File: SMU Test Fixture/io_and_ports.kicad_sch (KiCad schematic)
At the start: 50 parts, among them J1 AD2 Connector, J10 Ext. Source, J12 105-1102-001, J2 Scope -1, J3 Scope +1, J4 Scope -2, J5 Scope +2, J6 WG1, J7 WG2, J8 AD2 Connector, J9 105-1102-001, U10 ADGS1412, U11 ADGS1412, U8 ADGS1412, U9 ADGS1412

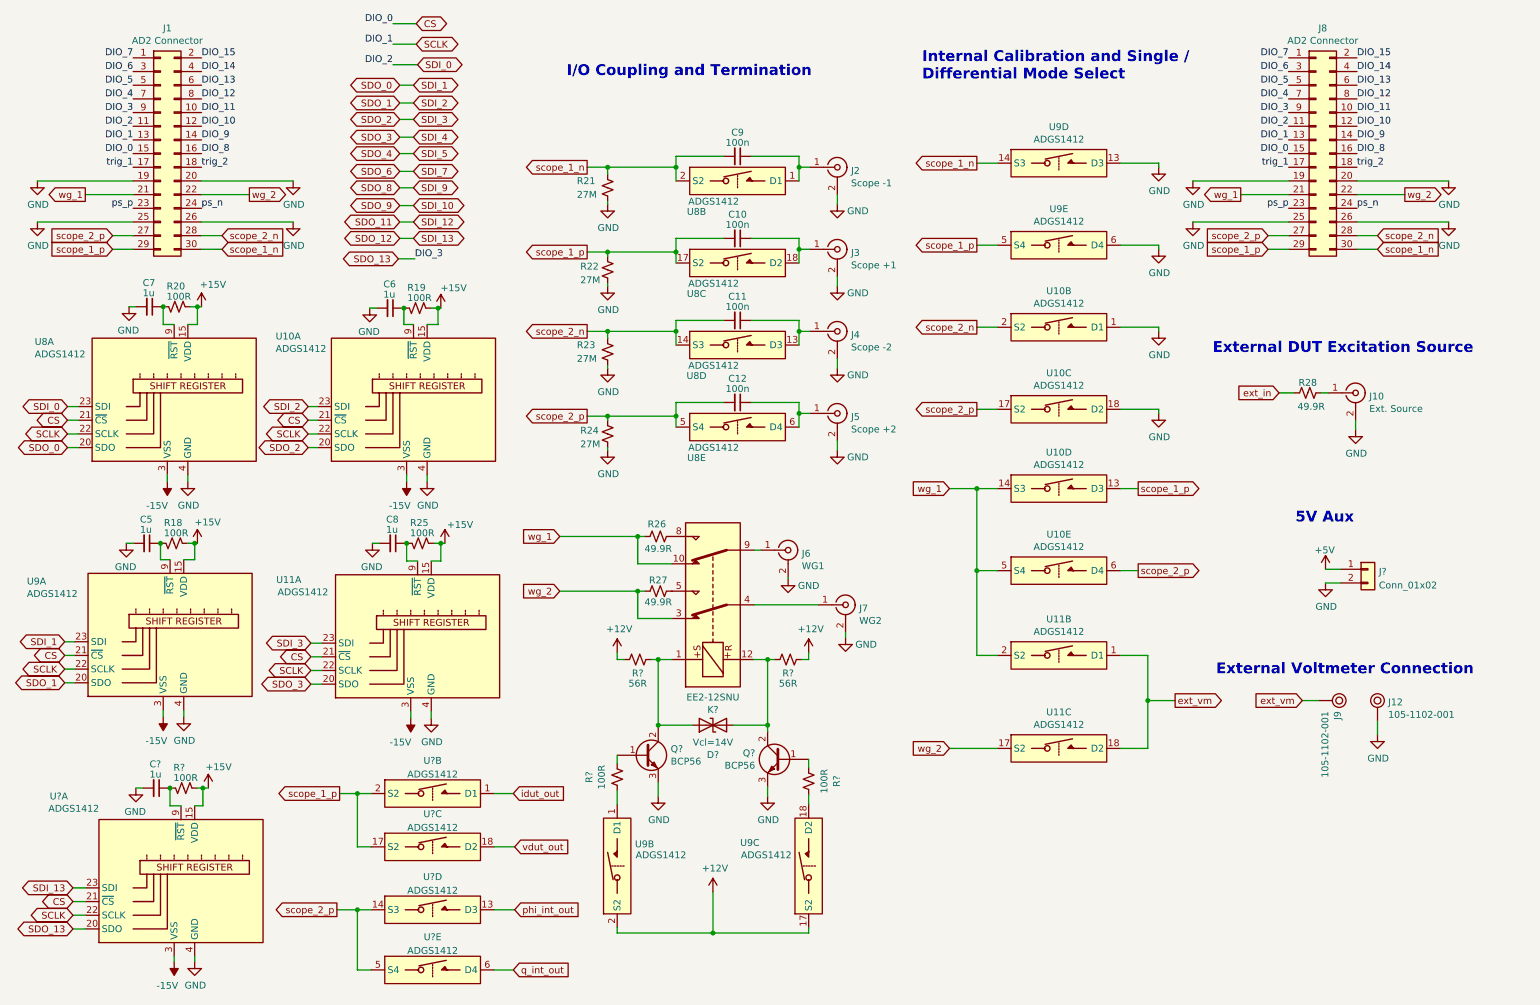
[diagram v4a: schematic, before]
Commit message: Finish adding bypass for all a.switches
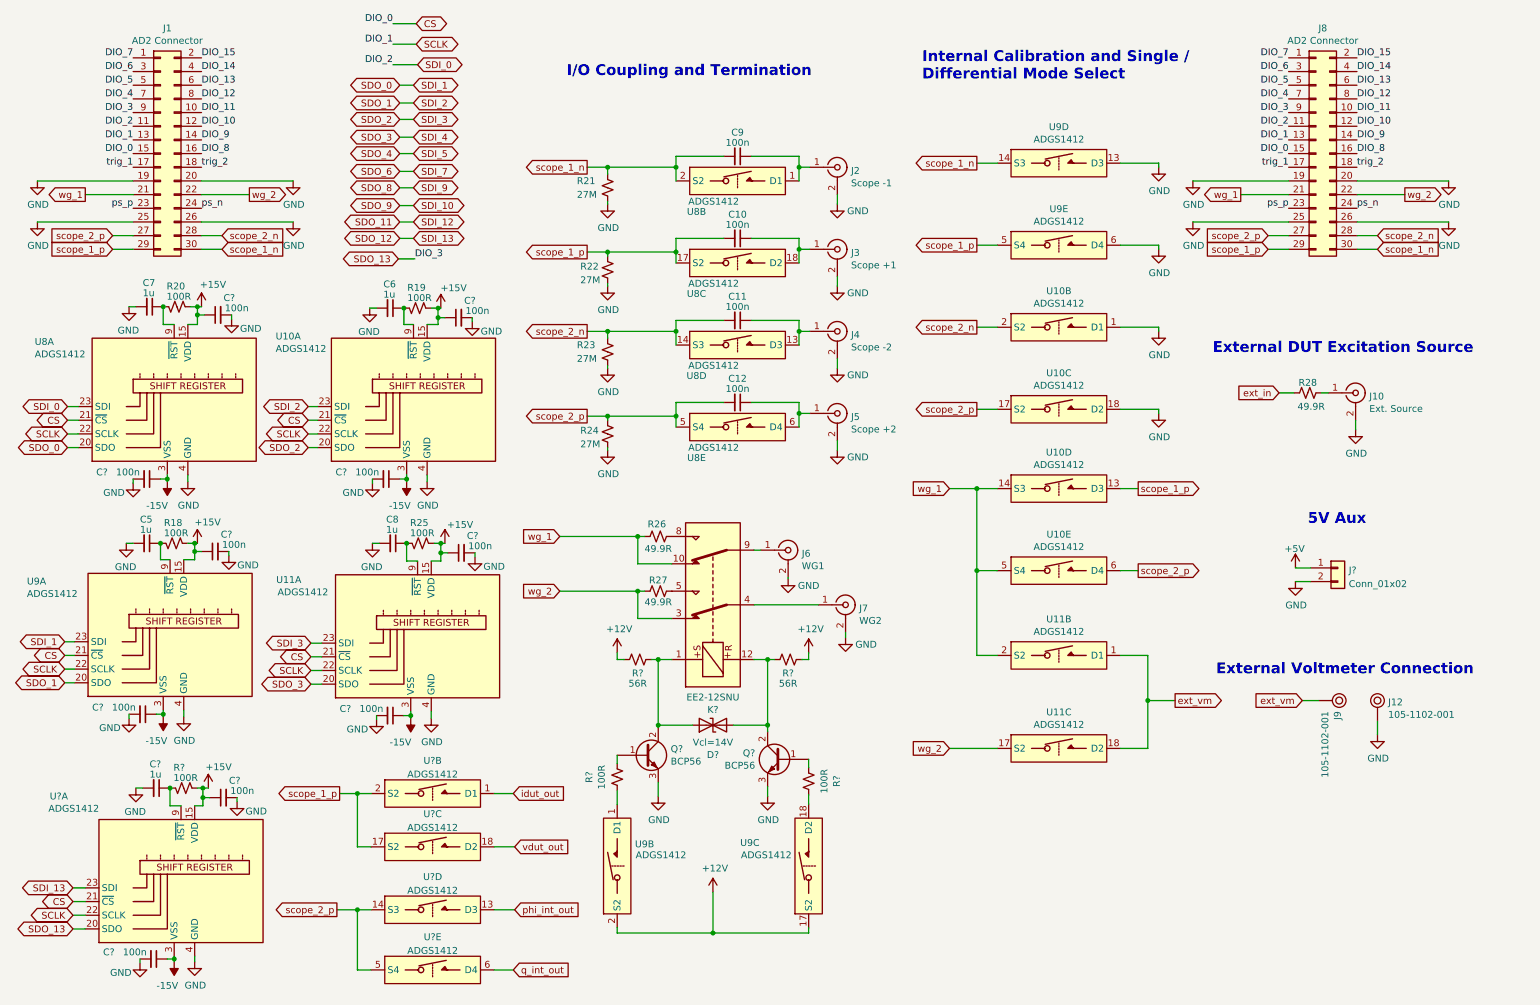
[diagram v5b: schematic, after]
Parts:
- added C? (x10): 100n, Capacitor_SMD:C_0805_2012Metric_Pad1.18x1.45mm_HandSolder, symbol Device:C_Small
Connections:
- net +15V: now also C?.1, C?.1, C?.1, C?.1, C?.1
- net -15V: now also C?.1, C?.1, C?.1, C?.1, C?.1
- net GND: now also C?.2, C?.2, C?.2, C?.2, C?.2, C?.2, C?.2, C?.2, C?.2, C?.2
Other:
- moved on the sheet: J?

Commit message: Split ADGS1408 units, add switch contorl page
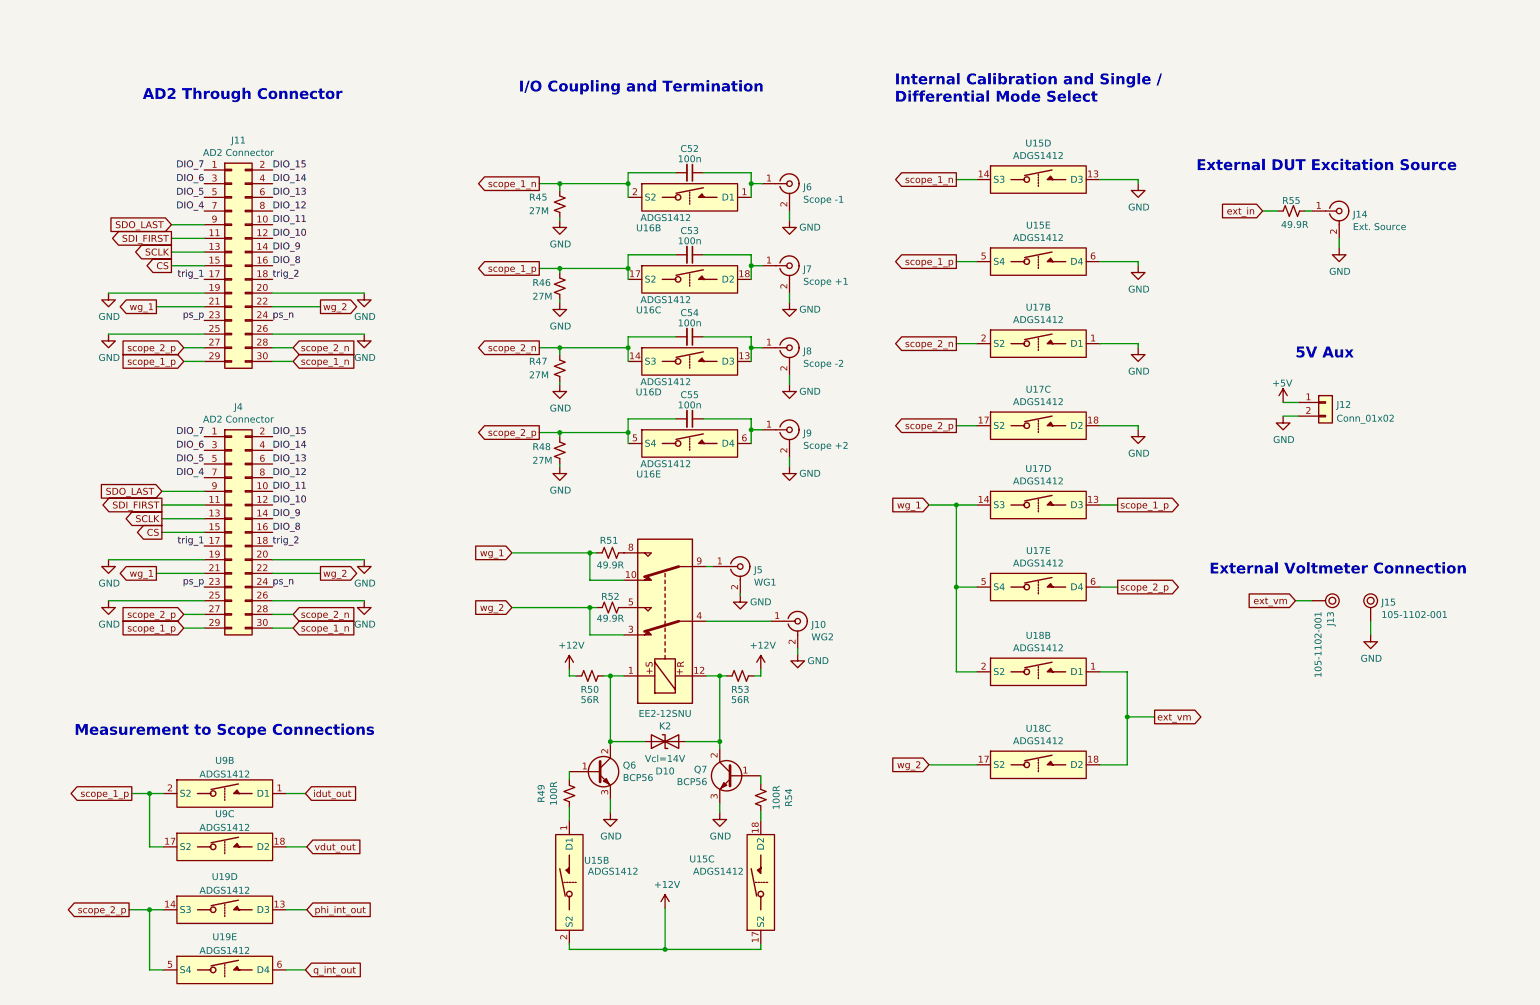
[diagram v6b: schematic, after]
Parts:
- removed C5, C6, C7, C8, C?: 1u, symbol Device:C_Small
- removed C? (x10): 100n, Capacitor_SMD:C_0805_2012Metric_Pad1.18x1.45mm_HandSolder, symbol Device:C_Small
- removed R18, R19, R20, R25, R?: 100R, symbol Device:R_Small_US
- removed unit 1 of U10
- removed unit 1 of U11
- removed unit 1 of U8
- removed unit 1 of U9
- removed U?: ADGS1412, Package_CSP:LFCSP-24-1EP_4x4mm_P0.5mm_EP2.5x2.5mm, symbol SMUTestFixture-rescue:ADGS1412-MAGI_Symbols
- gave numbers to parts that had none: 11
- renumbered C9 to C52, C10 to C53, C11 to C54, C12 to C55, J7 to J10, J8 to J11, J9 to J13, J10 to J14, J12 to J15, J1 to J4, J6 to J5, J2 to J6, J3 to J7, J4 to J8, J5 to J9, R21 to R45, R22 to R46, R23 to R47, R24 to R48, R26 to R51, R27 to R52, R28 to R55, U9 to U15, U8 to U16, U10 to U17, U11 to U18
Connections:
- net SDI_0 renamed SDI_FIRST
- net SDO_13 renamed SDO_LAST
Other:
- note added: "AD2 Through Connector"
- note added: "Measurement to Scope Connections"
- moved on the sheet: C52, C53, C54, C55, D10, J10, J11, J12, J13, J14, J15, J4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

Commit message: Symbol fixes, ERC pass
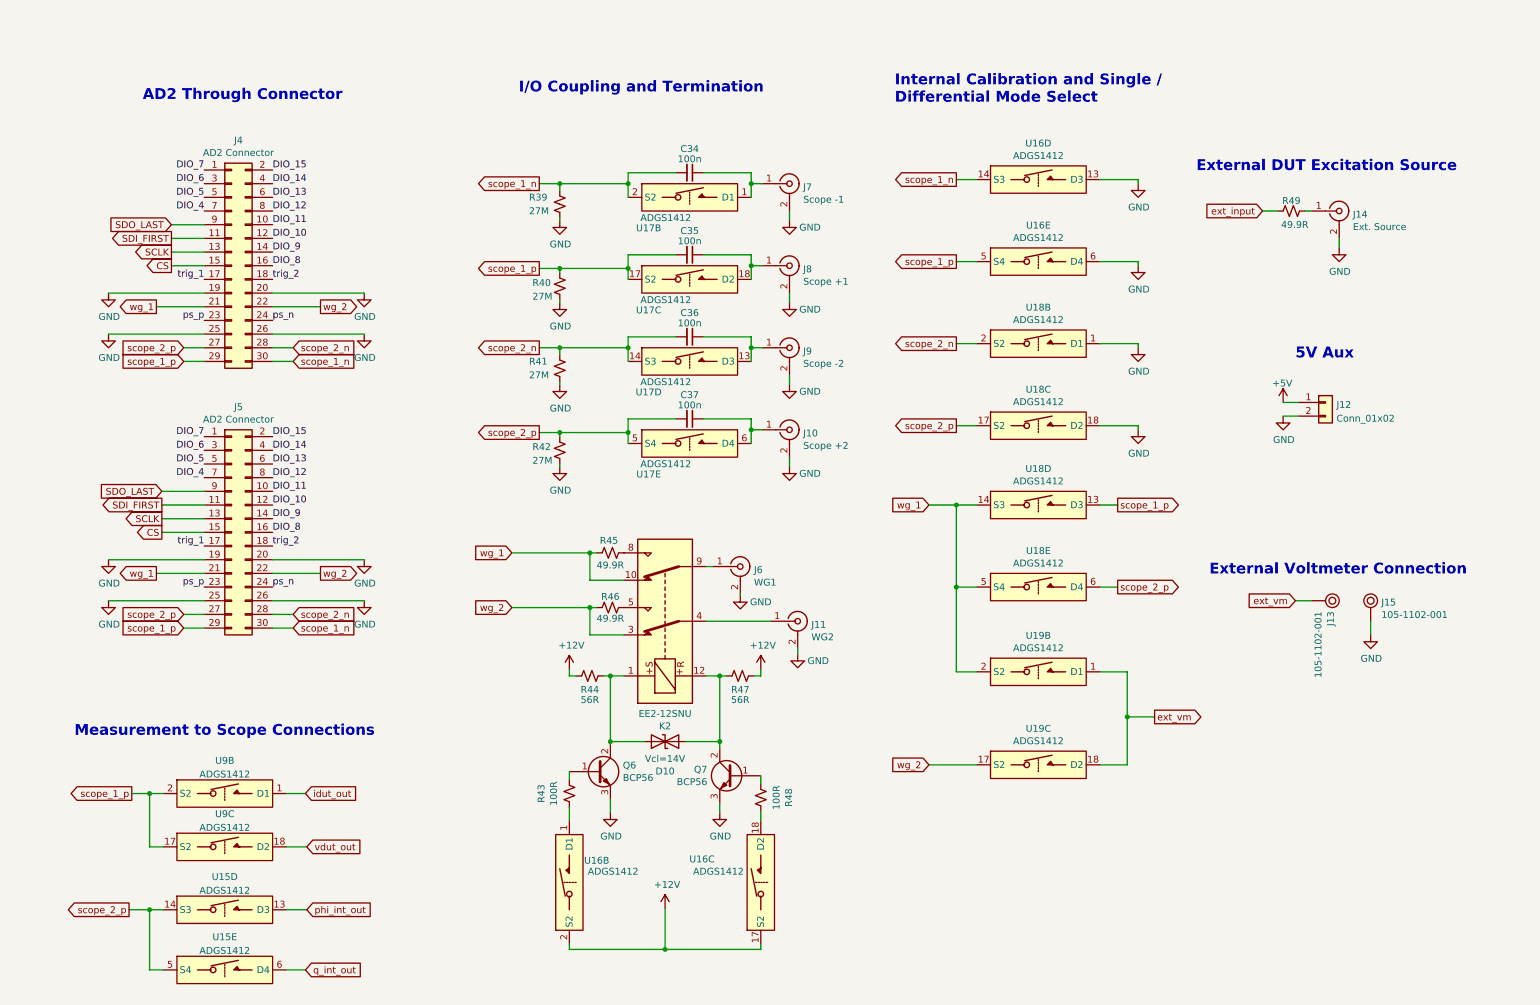
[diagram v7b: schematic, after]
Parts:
- renumbered C52 to C34, C53 to C35, C54 to C36, C55 to C37, J9 to J10, J10 to J11, J11 to J4, J4 to J5, J5 to J6, J6 to J7, J7 to J8, J8 to J9, R45 to R39, R46 to R40, R47 to R41, R48 to R42, R49 to R43, R50 to R44, R51 to R45, R52 to R46, R53 to R47, R54 to R48, R55 to R49, U19 to U15, U15 to U16, U16 to U17, U17 to U18, U18 to U19
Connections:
- net ext_in renamed ext_input
